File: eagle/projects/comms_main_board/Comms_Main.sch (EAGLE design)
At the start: 132 parts, among them J10 MOL-KK-2-RA, J11 MOL-KK-3P-RA, J12 MOL-KK-3P-RA, J13 MOL-KK-3P-RA, J14 MOL-KK-3P-RA, J15 MOL-KK-2-RA, J16 MOLKK_POW_2_RA, J17 MOLKK_POW_2_RA, J18 MOLKK_POW_2_RA, J19 MOLKK_POW_2_RA, J2 PRT-12639, J20 MOL-KK-2-RA, J3 PRT-12639, J4 PRT-12639, J5 PRT-12639, J6 MOL-KK-3P-RA, J7 MOL-KK-5P-V, J8 RECEPTACLE-2x20-254MM, J9 MOL-KK-3P-RA, Q1 CSD17579Q3A, U1 TPS562209DDCT, U11 TPS562209DDCT, U14 MAX4311, U2 LP2985-33DBVR, U3 LP5900TLX-3.3/NOPB, U4 TPS562209DDCT, U5 LMZ34002RKGR, U6 LM3488MMX/NOPB, U7 PCT2075D,118, U8 MS560702BA03-50, U9 MAX-M8Q

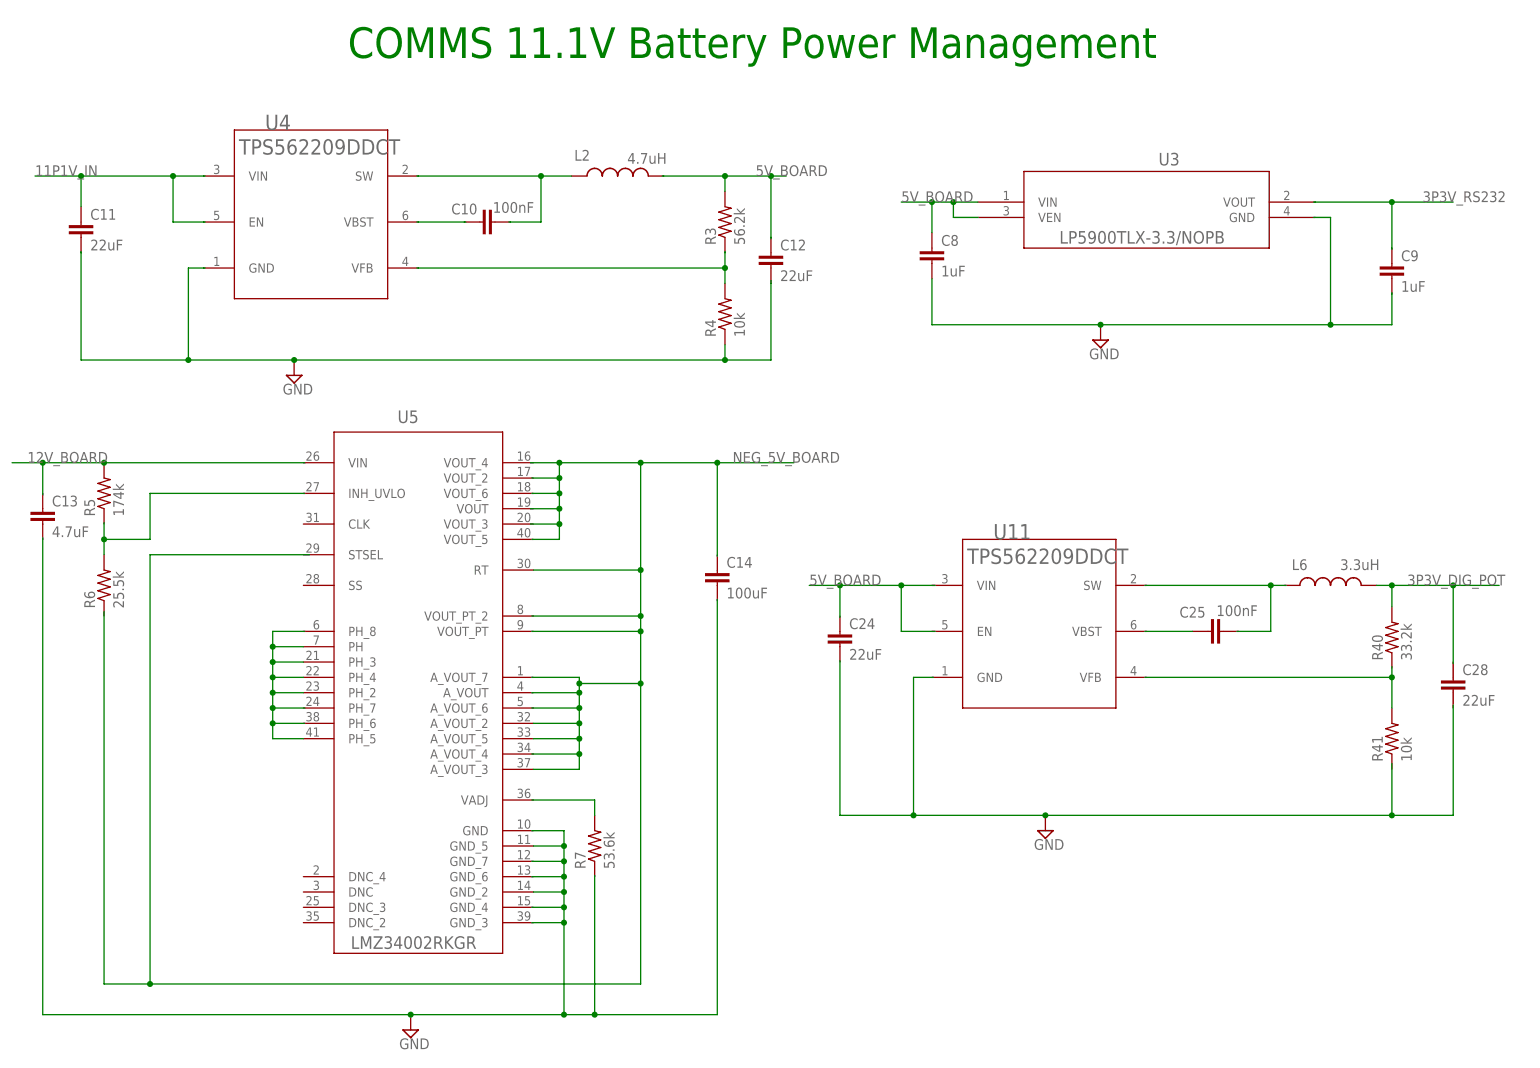
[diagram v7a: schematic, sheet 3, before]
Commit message: Fixing DRCs, so we can start a PCB layout
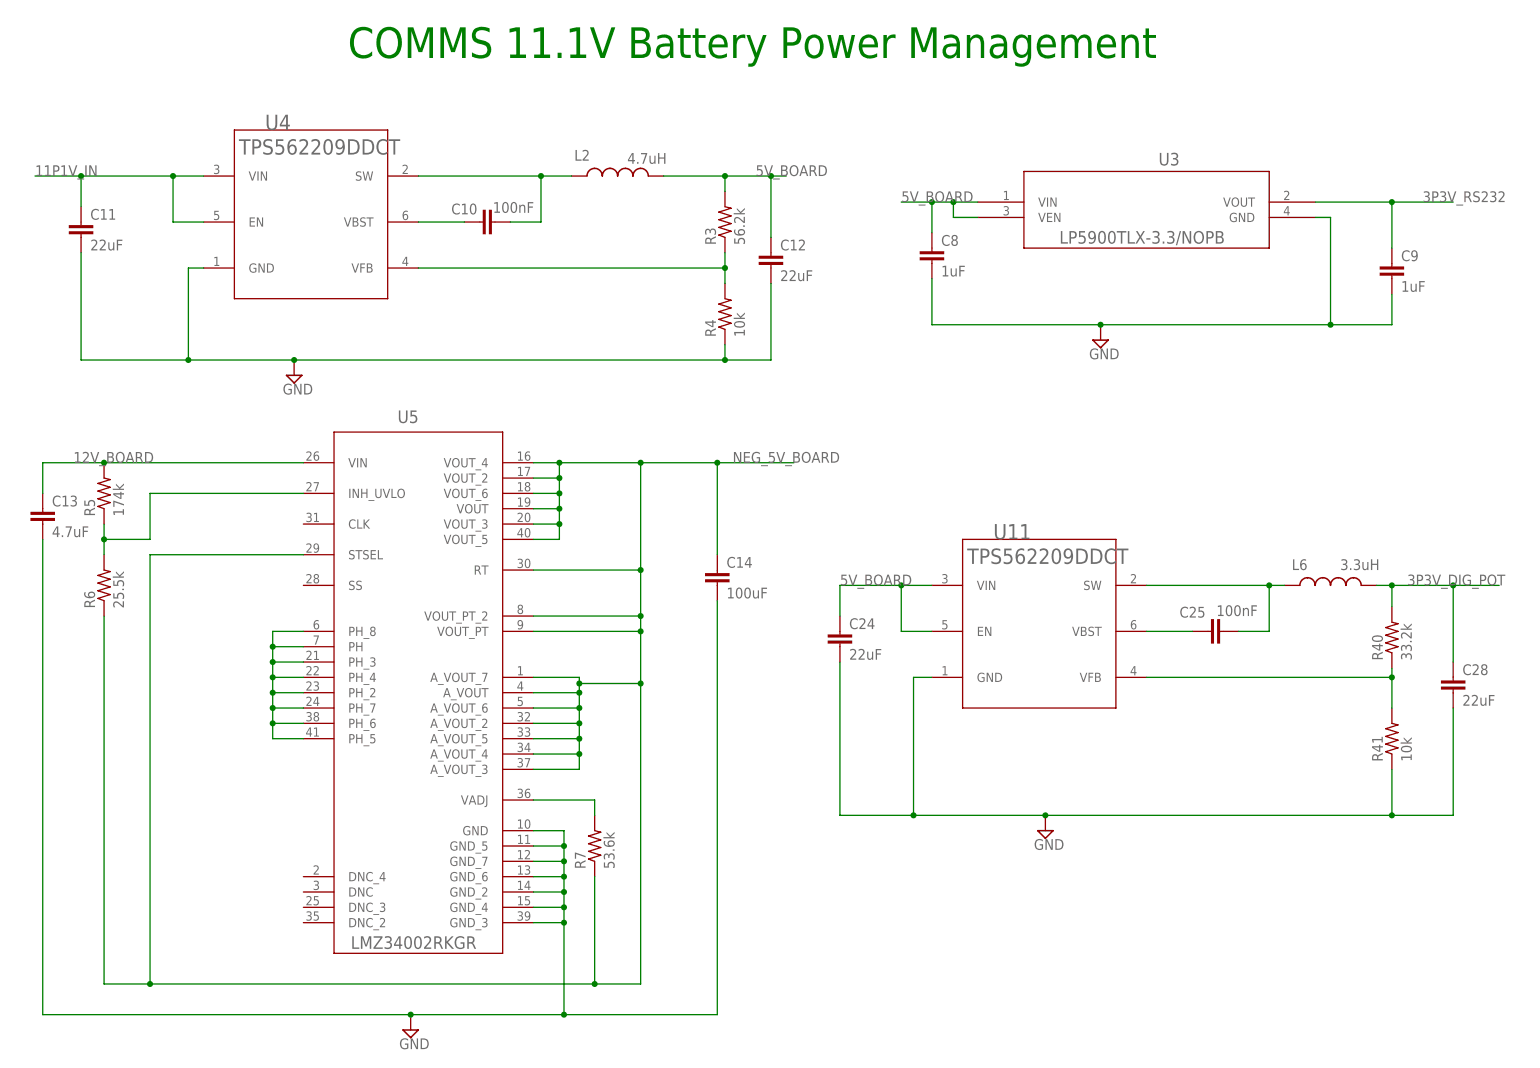
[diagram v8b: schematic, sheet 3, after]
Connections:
- new net MISO: J7.3, J8.21
- new net MOSI: J7.4, J8.19
- new net N$21: R12.1, R13.2, U6.FB
- new net N$61: C25.1, U11.VBST
- new net N$62: U13.T2OUT
- new net N$65: U13.R1IN
- new net N$66: U13.R2IN
- new net N$67: U13.T2IN
- new net N$68: U13.R1OUT
- new net N$69: U13.R2OUT
- new net POT_HVC: R15.1
- new net SCLK: J7.2, J8.23
- new net SS: J7.1, J8.24
- new net UART_RXD: J8.10
- net 12V_BOARD: now also C13.1, R12.2, U5.VIN
- net 3P3V_DIG_POT: now also C28.1
- net 5V_BOARD: now also C24.1, J11.2, J12.2, J13.2, J14.2, U11.EN, U11.VIN
- net 5V_PI: now also J8.2
- net GND: now also C13.2, C14.2, C21.2, C24.2, C28.2, C29.2, J10.2, J11.3, J12.3, J13.3, J14.3, J6.3, J7.5, J8.14, J8.20, J8.25, J8.30, J8.34, J8.39, J8.6, J8.9, R13.1, R14.1, R41.1, U10.VSS, U11.GND, U5.GND, U5.GND_3, U5.GND_4, U5.GND_6, U5.GND_7
- net GPIO_MUX_ADDR0: now also J8.11
- net GPIO_MUX_ADDR1: now also J8.13
- net N$1: now also C1.1
- net N$10: now also U5.VADJ
- net N$11: now also U5.PH_6, U5.PH_7, U5.PH_8
- net N$19: now also C20.2
- net N$48: now also R40.1, U11.VFB
- net N$50: now also R14.2, U10.HVC/A0
- net N$8: now also C25.2, L6.1, U11.SW; no longer C25.1
- net N$9: now also R5.1, U5.INH_UVLO
- net NEG_5V_BOARD: now also C14.1, R6.1, R7.1, U5.A_VOUT, U5.A_VOUT_4, U5.A_VOUT_6, U5.A_VOUT_7, U5.STSEL, U5.VOUT, U5.VOUT_2, U5.VOUT_3, U5.VOUT_4, U5.VOUT_5, U5.VOUT_6, U5.VOUT_PT, U5.VOUT_PT_2
- net OSD_DATA: now also J10.1
- net POT_A: now also U10.P0A
- net POT_B: now also U10.P0B
- net POT_W: now also U10.P0W
- net PTT_GPIO: now also J8.36
- net SCL: now also J6.2, J8.28
- net SDA: now also J6.1, J8.27
- net UART_TXD: now also J8.8
- net VID_IN0: now also J11.1
- net VID_IN1: now also J12.1
- net VID_IN2: now also J13.1
- net VID_IN3: now also J14.1
